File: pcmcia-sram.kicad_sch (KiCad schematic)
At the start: 2 parts, among them J1 Conn_02x34_Top_Bottom

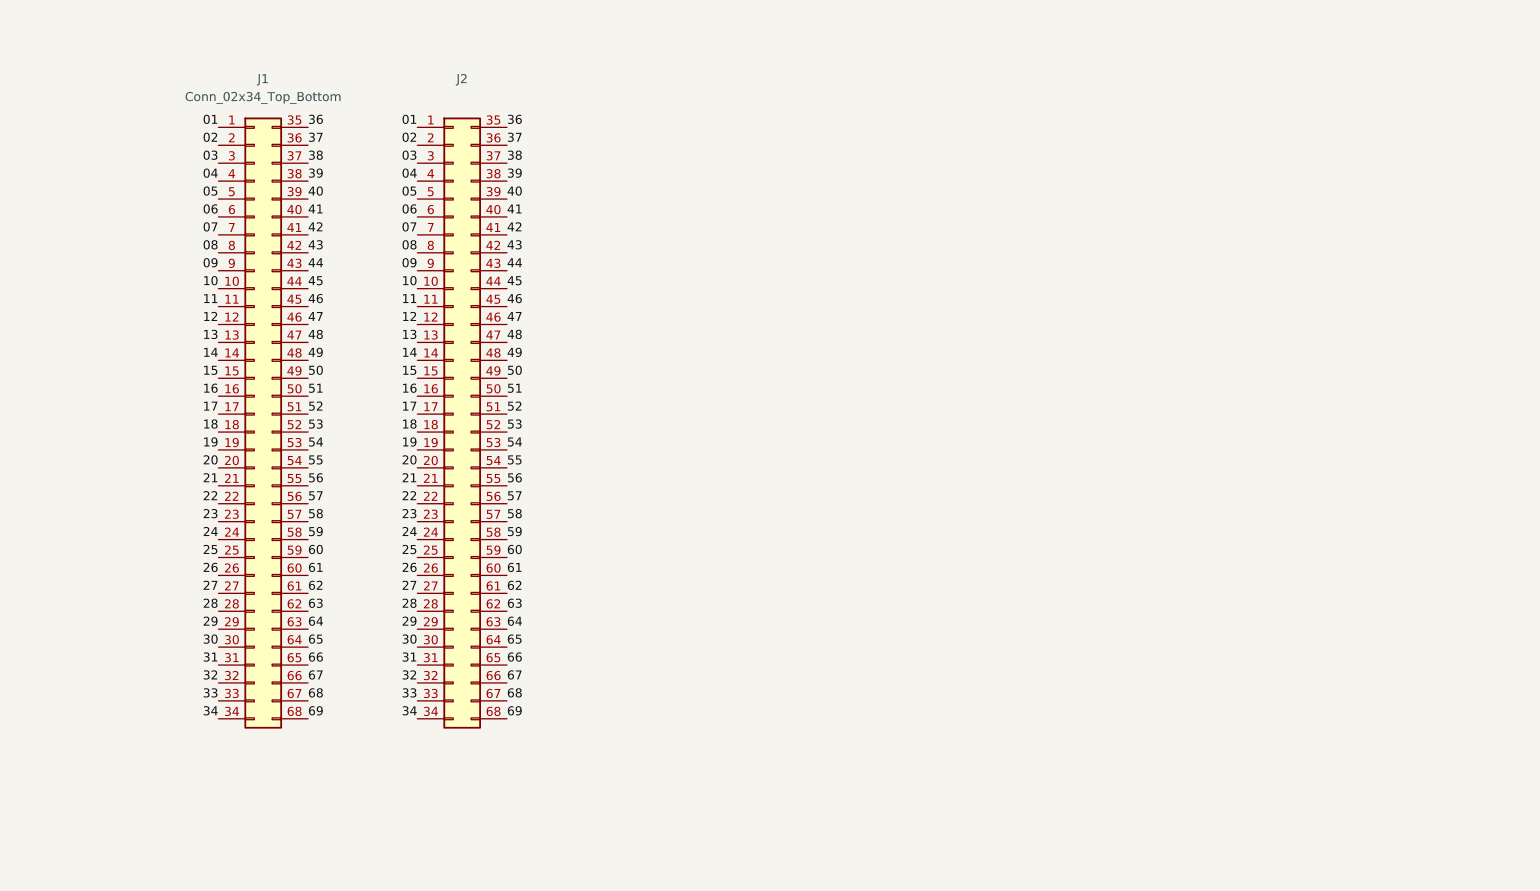
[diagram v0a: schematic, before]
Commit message: Schematic done
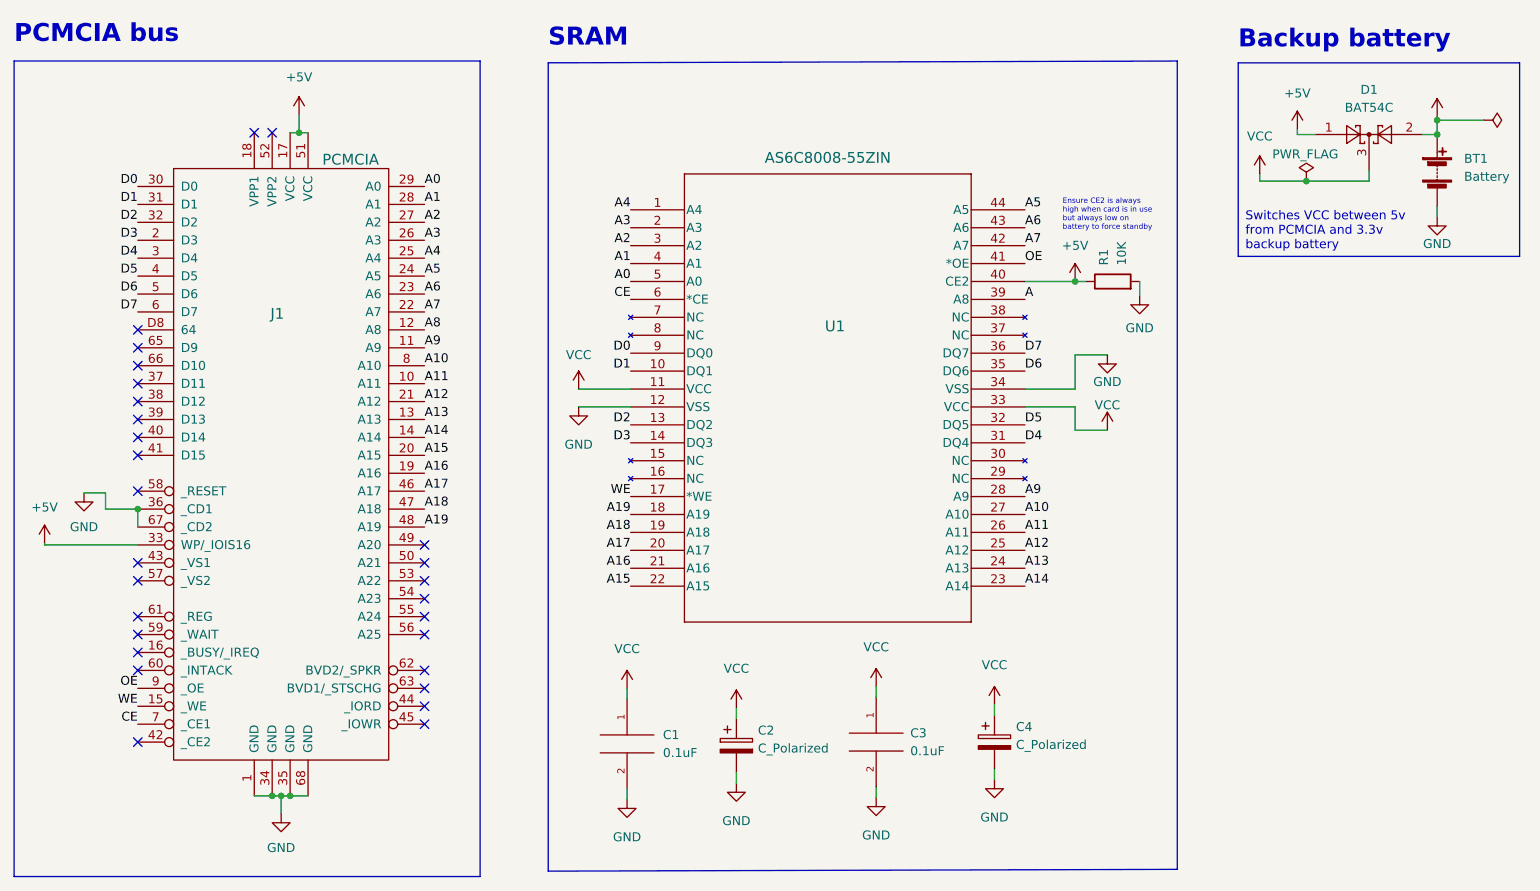
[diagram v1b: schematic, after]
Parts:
- removed J1: Conn_02x34_Top_Bottom, Connector_PinHeader_2.54mm:PinHeader_2x34_P2.54mm_Vertical, symbol Connector_Generic:Conn_02x34_Top_Bottom
- removed J2: (no value), symbol Connector_Generic:Conn_02x34_Top_Bottom
- added BT1: Battery, Battery:Battery_Panasonic_CR2032-VS1N_Vertical_CircularHoles, symbol Device:Battery
- added C1, C3: 0.1uF, Capacitor_SMD:C_0805_2012Metric_Pad1.18x1.45mm_HandSolder, symbol pspice:C
- added C2, C4: C_Polarized, Capacitor_SMD:C_1206_3216Metric_Pad1.33x1.80mm_HandSolder, symbol Device:C_Polarized
- added D1: BAT54C, Package_TO_SOT_SMD:SOT-23, symbol Diode:BAT54C
- added J1: PCMCIA, symbol pcmcia:PCMCIA
- added R1: 10K, Resistor_SMD:R_0805_2012Metric_Pad1.20x1.40mm_HandSolder, symbol Device:R
- added U1: AS6C8008-55ZIN, Package_SO:TSOP-II-44_10.16x18.41mm_P0.8mm, symbol pcmcia:AS6C8008-55ZIN
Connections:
- new net +5V: D1.1, J1.17 (VCC), J1.33 (WP/_IOIS16), J1.51 (VCC), R1.1, U1.40 (CE2)
- new net +BATT: BT1.1 (+), D1.2
- new net A: U1.39 (A8)
- new net A0: J1.29 (A0), U1.5 (A0)
- new net A1: J1.28 (A1), U1.4 (A1)
- new net A10: J1.8 (A10), U1.27 (A10)
- new net A11: J1.10 (A11), U1.26 (A11)
- new net A12: J1.21 (A12), U1.25 (A12)
- new net A13: J1.13 (A13), U1.24 (A13)
- new net A14: J1.14 (A14), U1.23 (A14)
- new net A15: J1.20 (A15), U1.22 (A15)
- new net A16: J1.19 (A16), U1.21 (A16)
- new net A17: J1.46 (A17), U1.20 (A17)
- new net A18: J1.47 (A18), U1.19 (A18)
- new net A19: J1.48 (A19), U1.18 (A19)
- new net A2: J1.27 (A2), U1.3 (A2)
- new net A3: J1.26 (A3), U1.2 (A3)
- new net A4: J1.25 (A4), U1.1 (A4)
- new net A5: J1.24 (A5), U1.44 (A5)
- new net A6: J1.23 (A6), U1.43 (A6)
- new net A7: J1.22 (A7), U1.42 (A7)
- new net A8: J1.12 (A8)
- new net A9: J1.11 (A9), U1.28 (A9)
- new net CE: J1.7 (_CE1), U1.6 (*CE)
- new net D0: J1.30 (D0), U1.9 (DQ0)
- new net D1: J1.31 (D1), U1.10 (DQ1)
- new net D2: J1.32 (D2), U1.13 (DQ2)
- new net D3: J1.2 (D3), U1.14 (DQ3)
- new net D4: J1.3 (D4), U1.31 (DQ4)
- new net D5: J1.4 (D5), U1.32 (DQ5)
- new net D6: J1.5 (D6), U1.35 (DQ6)
- new net D7: J1.6 (D7), U1.36 (DQ7)
- new net GND: BT1.2 (-), C1.2, C2.2, C3.2, C4.2, J1.1 (GND), J1.34 (GND), J1.35 (GND), J1.36 (_CD1), J1.67 (_CD2), J1.68 (GND), R1.2, U1.12 (VSS), U1.34 (VSS)
- new net OE: J1.9 (_OE), U1.41 (*OE)
- new net VCC: C1.1, C2.1, C3.1, C4.1, D1.3, U1.11 (VCC), U1.33 (VCC)
- new net WE: J1.15 (_WE), U1.17 (*WE)
- no-connect marks 0 -> 28
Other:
- note added: "Backup battery"
- note added: "Ensure CE2 is always high when card is in use but always low on battery to force standby"
- note added: "PCMCIA bus"
- note added: "SRAM"
- note added: "Switches VCC between 5v from PCMCIA and 3.3v backup battery"
- title: (none) -> PCMCIA SRAM card

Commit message: Fixed address pin
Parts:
- J1: footprint (none) -> pcmcia:pcmcia
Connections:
- net A is gone; now on net A8: U1.39 (A8)
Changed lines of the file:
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@@
     (effects (font (size 1.27 1.27)) (justify right bottom))
   )
-  (label "A" (at 160.02 56.642 0)
+  (label "A8" (at 160.02 56.642 0)
     (effects (font (size 1.27 1.27)) (justify left bottom))
   )
@@
       (effects (font (size 1.27 1.27)) hide)
     )
-    (property "Value" "" (id 1) (at 228.854 26.416 0)
+    (property "Value" "PWR_FLAG" (id 1) (at 228.854 26.416 0)
       (effects (font (size 1.27 1.27)) (justify left))
     )
@@
       (effects (font (size 1.524 1.524)) (justify left))
     )
-    (property "Footprint" "" (id 2) (at 54.61 63.5 0)
+    (property "Footprint" "pcmcia:pcmcia" (id 2) (at 54.61 63.5 0)
       (effects (font (size 1.524 1.524)) hide)
     )
@@
       (effects (font (size 1.27 1.27)) hide)
     )
-    (property "Value" "" (id 1) (at 218.44 25.4 0))
+    (property "Value" "+BATT" (id 1) (at 218.44 25.4 0))
     (property "Footprint" "" (id 2) (at 218.44 30.734 0)
       (effects (font (size 1.27 1.27)) hide)

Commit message: Various fixes
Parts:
- CR2032: renamed from BT1; footprint Battery:Battery_Panasonic_CR2032-VS1N_Vertical_CircularHoles -> pcmcia:BAT_BAT-HLD-001; symbol Device:Battery -> pcmcia:BAT-HLD-001
- U1: value AS6C8008-55ZIN -> (none); footprint Package_SO:TSOP-II-44_10.16x18.41mm_P0.8mm -> (none)
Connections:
- net +BATT: now also CR2032.P1, CR2032.P2; no longer CR2032.1 (+)
- net GND: now also CR2032.N1; no longer CR2032.2 (-)
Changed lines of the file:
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@@
     (stroke (width 0) (type default) (color 0 0 0 0))
   )
-  (wire (pts (xy 218.44 31.242) (xy 225.044 31.242))
+  (wire (pts (xy 218.44 31.242) (xy 220.472 31.242))
     (stroke (width 0) (type default) (color 0 0 0 0))
   )
@@
     (stroke (width 0) (type default) (color 0 0 0 0))
   )
-  (polyline (pts (xy 190.246 23.114) (xy 190.246 50.546))
+  (polyline (pts (xy 190.246 23.114) (xy 190.5 54.102))
     (stroke (width 0) (type default) (color 0 0 0 0))
   )
@@
     (stroke (width 0) (type default) (color 0 0 0 0))
   )
-  (polyline (pts (xy 230.124 50.546) (xy 230.124 23.114))
+  (polyline (pts (xy 230.378 54.102) (xy 230.124 23.114))
     (stroke (width 0) (type default) (color 0 0 0 0))
   )
@@
     (stroke (width 0) (type default) (color 0 0 0 0))
   )
-  (wire (pts (xy 218.44 43.434) (xy 218.44 44.958))
-    (stroke (width 0) (type default) (color 0 0 0 0))
-  )
   (polyline (pts (xy 16.764 22.86) (xy 82.804 22.86))
     (stroke (width 0) (type default) (color 0 0 0 0))
@@
     (stroke (width 0) (type default) (color 0 0 0 0))
   )
-  (polyline (pts (xy 190.246 50.546) (xy 230.124 50.546))
+  (polyline (pts (xy 190.5 54.102) (xy 230.378 54.102))
+    (stroke (width 0) (type default) (color 0 0 0 0))
+  )
+  (wire (pts (xy 218.44 48.514) (xy 224.028 48.514))
     (stroke (width 0) (type default) (color 0 0 0 0))
   )
@@
   )
   (text "Switches VCC between 5v \nfrom PCMCIA and 3.3v \nbackup battery"
-    (at 191.262 49.784 0)
+    (at 191.262 53.34 0)
     (effects (font (size 1.27 1.27)) (justify left bottom))
   )
@@
     (effects (font (size 1.27 1.27)) (justify left bottom))
   )
-  (symbol (lib_id "power:PWR_FLAG") (at 225.044 31.242 270) (unit 1)
+  (symbol (lib_id "power:PWR_FLAG") (at 220.472 31.242 270) (unit 1)
     (in_bom yes) (on_board yes)
-    (property "Reference" "#FLG0101" (id 0) (at 226.949 31.242 0)
-      (effects (font (size 1.27 1.27)) hide)
-    )
-    (property "Value" "PWR_FLAG" (id 1) (at 228.854 26.416 0)
-      (effects (font (size 1.27 1.27)) (justify left))
-    )
-    (property "Footprint" "" (id 2) (at 225.044 31.242 0)
-      (effects (font (size 1.27 1.27)) hide)
-    )
-    (property "Datasheet" "~" (id 3) (at 225.044 31.242 0)
+    (property "Reference" "#FLG0101" (id 0) (at 222.377 31.242 0)
+      (effects (font (size 1.27 1.27)) hide)
+    )
+    (property "Value" "PWR_FLAG" (id 1) (at 224.282 26.416 0)
+      (effects (font (size 1.27 1.27)) (justify left))
+    )
+    (property "Footprint" "" (id 2) (at 220.472 31.242 0)
+      (effects (font (size 1.27 1.27)) hide)
+    )
+    (property "Datasheet" "~" (id 3) (at 220.472 31.242 0)
       (effects (font (size 1.27 1.27)) hide)
     )
@@
     (pin "62")
     (pin "63")
+    (pin "64")
     (pin "65")
     (pin "66")
@@
     (pin "8")
     (pin "9")
-    (pin "D8")
   )
   (symbol (lib_id "Device:C_Polarized") (at 119.126 119.888 0) (unit 1)
@@
     (pin "2")
   )
-  (symbol (lib_id "Device:Battery") (at 218.44 38.354 0) (unit 1)
+  (symbol (lib_id "pcmcia:BAT-HLD-001") (at 218.44 40.894 270) (unit 1)
     (in_bom yes) (on_board yes)
-    (property "Reference" "BT1" (id 0) (at 222.25 36.7029 0)
-      (effects (font (size 1.27 1.27)) (justify left))
-    )
-    (property "Value" "Battery" (id 1) (at 222.25 39.2429 0)
-      (effects (font (size 1.27 1.27)) (justify left))
-    )
-    (property "Footprint" "Battery:Battery_Panasonic_CR2032-VS1N_Vertical_CircularHoles" (id 2) (at 210.058 58.166 90)
-      (effects (font (size 1.27 1.27)) hide)
-    )
-    (property "Datasheet" "~" (id 3) (at 218.44 36.83 90)
-      (effects (font (size 1.27 1.27)) hide)
-    )
-    (pin "1")
-    (pin "2")
+    (property "Reference" "CR2032" (id 0) (at 220.0911 44.704 0)
+      (effects (font (size 1.27 1.27)) (justify left))
+    )
+    (property "Value" "Battery" (id 1) (at 224.028 37.338 0)
+      (effects (font (size 1.27 1.27)) (justify left))
+    )
+    (property "Footprint" "pcmcia:BAT_BAT-HLD-001" (id 2) (at 218.44 40.894 0)
+      (effects (font (size 1.27 1.27)) (justify bottom) hide)
+    )
+    (property "Datasheet" "~" (id 3) (at 218.44 40.894 0)
+      (effects (font (size 1.27 1.27)) hide)
+    )
+    (pin "N1")
+    (pin "P1")
+    (pin "P2")
   )
   (symbol (lib_id "power:+5V") (at 167.132 54.102 0) (unit 1)
@@
       (effects (font (size 1.524 1.524)))
     )
-    (property "Value" "AS6C8008-55ZIN" (id 1) (at 132.08 36.576 0)
+    (property "Value" "" (id 1) (at 132.08 36.576 0)
       (effects (font (size 1.524 1.524)))
     )
-    (property "Footprint" "Package_SO:TSOP-II-44_10.16x18.41mm_P0.8mm" (id 2) (at 104.14 43.942 0)
+    (property "Footprint" "" (id 2) (at 104.14 43.942 0)
       (effects (font (size 1.27 1.27) italic) hide)
     )
@@
     (pin "1")
   )
-  (symbol (lib_id "power:GND") (at 218.44 44.958 0) (unit 1)
+  (symbol (lib_id "power:GND") (at 224.028 48.514 0) (unit 1)
     (in_bom yes) (on_board yes)
-    (property "Reference" "#PWR0106" (id 0) (at 218.44 51.308 0)
-      (effects (font (size 1.27 1.27)) hide)
-    )
-    (property "Value" "GND" (id 1) (at 218.44 48.768 0))
-    (property "Footprint" "" (id 2) (at 218.44 44.958 0)
-      (effects (font (size 1.27 1.27)) hide)
-    )
-    (property "Datasheet" "" (id 3) (at 218.44 44.958 0)
+    (property "Reference" "#PWR0106" (id 0) (at 224.028 54.864 0)
+      (effects (font (size 1.27 1.27)) hide)
+    )
+    (property "Value" "GND" (id 1) (at 224.028 52.324 0))
+    (property "Footprint" "" (id 2) (at 224.028 48.514 0)
+      (effects (font (size 1.27 1.27)) hide)
+    )
+    (property "Datasheet" "" (id 3) (at 224.028 48.514 0)
       (effects (font (size 1.27 1.27)) hide)
     )
@@
       (reference "#PWR0123") (unit 1) (value "VCC") (footprint "")
     )
-    (path "/4c85df79-9da1-4fa2-8203-0afdc5058a6d"
-      (reference "BT1") (unit 1) (value "Battery") (footprint "Battery:Battery_Panasonic_CR2032-VS1N_Vertical_CircularHoles")
-    )
     (path "/d39ee884-67d6-47a3-8a38-6186f16b0611"
       (reference "C1") (unit 1) (value "0.1uF") (footprint "Capacitor_SMD:C_0805_2012Metric_Pad1.18x1.45mm_HandSolder")
@@
       (reference "C4") (unit 1) (value "C_Polarized") (footprint "Capacitor_SMD:C_1206_3216Metric_Pad1.33x1.80mm_HandSolder")
     )
+    (path "/4c85df79-9da1-4fa2-8203-0afdc5058a6d"
+      (reference "CR2032") (unit 1) (value "Battery") (footprint "pcmcia:BAT_BAT-HLD-001")
+    )
     (path "/ef17c8b9-a7a8-4a87-a9cb-810fba4015c7"

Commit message: Add new design
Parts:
- removed C4: C_Polarized, Capacitor_SMD:C_1206_3216Metric_Pad1.33x1.80mm_HandSolder, symbol Device:C_Polarized
- U1: value (none) -> AS6C8008-55ZIN; footprint (none) -> Package_SO:TSOP-II-44_10.16x18.41mm_P0.8mm
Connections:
- net +5V: no longer J1.33 (WP/_IOIS16), R1.1
- net GND: now also J1.33 (WP/_IOIS16); no longer R1.2
- net VCC: now also R1.2
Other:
- moved on the sheet: U1

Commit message: Revision 1.1
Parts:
- removed R1: 10K, Resistor_SMD:R_0805_2012Metric_Pad1.20x1.40mm_HandSolder, symbol Device:R
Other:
- note removed: "Ensure CE2 is always high when card is in use but always low on battery to force standby"
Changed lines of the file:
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@@
   (junction (at 34.29 88.9) (diameter 0) (color 0 0 0 0)
-  )
-  (junction (at 102.87 69.85) (diameter 0) (color 0 0 0 0)
   )
   (junction (at 57.15 33.02) (diameter 0) (color 0 0 0 0)
@@
     (stroke (width 0) (type default))
   )
-  (wire (pts (xy 102.87 69.85) (xy 113.03 69.85))
+  (wire (pts (xy 97.79 69.85) (xy 113.03 69.85))
     (stroke (width 0) (type default))
   )
@@
   )
   (wire (pts (xy 55.88 33.02) (xy 57.15 33.02))
-    (stroke (width 0) (type default))
-  )
-  (wire (pts (xy 97.79 69.85) (xy 102.87 69.85))
     (stroke (width 0) (type default))
   )
@@
   (text "PCMCIA bus" (at 16.764 20.574 0)
     (effects (font (size 2.54 2.54) (thickness 0.508) bold) (justify left bottom))
-  )
-  (text "Ensure CE2 is always \nhigh when card is in use\nbut always low on \nbattery to force standby"
-    (at 119.38 30.48 0)
-    (effects (font (size 0.762 0.762)) (justify left bottom))
   )
   (text "SRAM" (at 92.456 21.082 0)
@@
         )
       )
-    )
-  )
-  (symbol (lib_id "Device:R") (at 102.87 66.04 0) (unit 1)
-    (in_bom yes) (on_board yes) (dnp no) (fields_autoplaced)
-    (property "Reference" "R1" (at 105.41 64.77 0)
-      (effects (font (size 1.27 1.27)) (justify left))
-    )
-    (property "Value" "10K" (at 105.41 67.31 0)
-      (effects (font (size 1.27 1.27)) (justify left))
-    )
-    (property "Footprint" "Resistor_SMD:R_0805_2012Metric_Pad1.20x1.40mm_HandSolder" (at 101.092 66.04 90)
-      (effects (font (size 1.27 1.27)) hide)
-    )
-    (property "Datasheet" "~" (at 102.87 66.04 0)
-      (effects (font (size 1.27 1.27)) hide)
-    )
-    (pin "1")
-    (pin "2")
-    (instances
-      (project "pcmcia-sram"
-        (path "/e857610b-4434-4144-b04e-43c1ebdc5ceb"
-          (reference "R1") (unit 1)
-        )
-      )
